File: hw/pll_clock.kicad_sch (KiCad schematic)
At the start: 24 parts, among them J7 BNC, U7 5P49V6965, Y1 25MHz

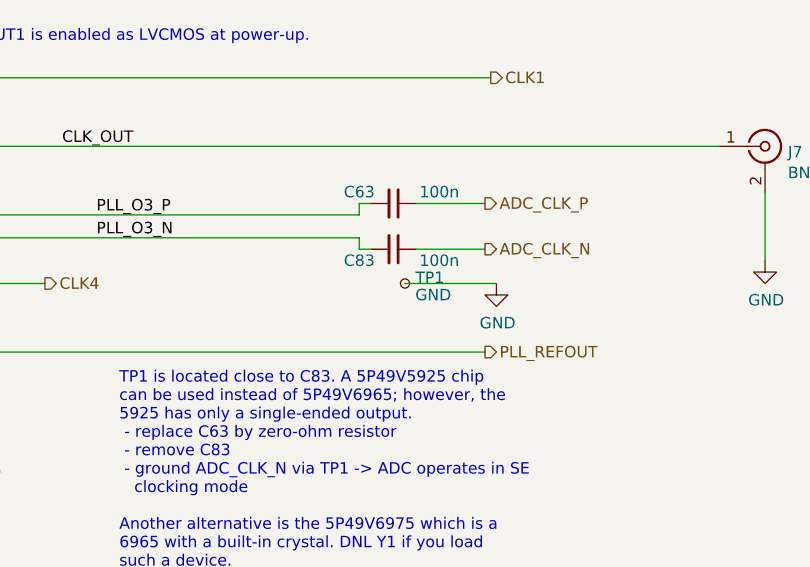
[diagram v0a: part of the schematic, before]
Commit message: updated parts assignments
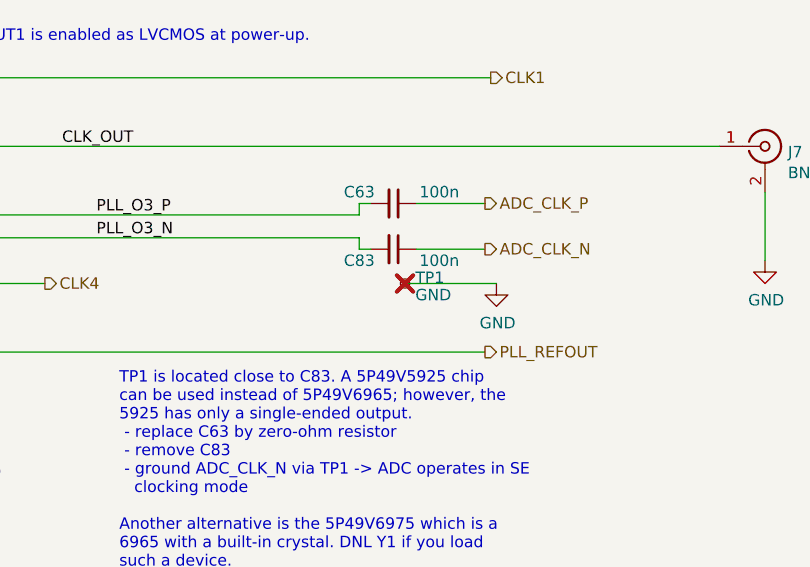
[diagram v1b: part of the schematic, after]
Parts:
- R11: Manufacturer (none) -> Stackpole; Part (none) -> RMCF0603FT2K94
- R118, R24, R27: Manufacturer (none) -> Stackpole; Part (none) -> RMCF0603FT33R0
- R17: Manufacturer (none) -> Stackpole; Part (none) -> RMCF0603FT301R
- R18: Manufacturer (none) -> Stackpole; Part (none) -> RMCF0603FT590R
- TP1: now not fitted; now left out of the parts list
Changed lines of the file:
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@@
 			)
 		)
-		(property "Part" ""
+		(property "Part" "RMCF0603FT33R0"
 			(at 163.83 81.28 90)
 			(effects
@@
 			)
 		)
-		(property "Manufacturer" ""
+		(property "Manufacturer" "Stackpole"
 			(at 163.83 81.28 90)
 			(effects
@@
 			)
 		)
-		(property "Datasheet" " ~"
+		(property "Datasheet" "~"
 			(at 254.635 81.28 0)
 			(effects
@@
 			)
 		)
-		(property "Part" ""
+		(property "Part" "RMCF0603FT33R0"
 			(at 163.83 73.66 90)
 			(effects
@@
 			)
 		)
-		(property "Manufacturer" ""
+		(property "Manufacturer" "Stackpole"
 			(at 163.83 73.66 90)
 			(effects
@@
 			)
 		)
-		(property "Part" ""
+		(property "Part" "RMCF0603FT33R0"
 			(at 163.83 96.52 90)
 			(effects
@@
 			)
 		)
-		(property "Manufacturer" ""
+		(property "Manufacturer" "Stackpole"
 			(at 163.83 96.52 90)
 			(effects
@@
 			)
 		)
-		(property "Part" ""
+		(property "Part" "RMCF0603FT301R"
 			(at 82.042 78.486 90)
 			(effects
@@
 			)
 		)
-		(property "Manufacturer" ""
+		(property "Manufacturer" "Stackpole"
 			(at 82.042 78.486 90)
 			(effects
@@
 			)
 		)
-		(property "Part" ""
+		(property "Part" "RMCF0603FT590R"
 			(at 82.042 71.12 90)
 			(effects
@@
 			)
 		)
-		(property "Manufacturer" ""
+		(property "Manufacturer" "Stackpole"
 			(at 82.042 71.12 90)
 			(effects
@@
 		(unit 1)
 		(exclude_from_sim no)
-		(in_bom yes)
-		(on_board yes)
-		(dnp no)
+		(in_bom no)
+		(on_board yes)
+		(dnp yes)
 		(fields_autoplaced yes)
 		(property "Reference" "TP1"
@@
 			)
 		)
-		(property "Part" ""
+		(property "Part" "RMCF0603FT2K94"
 			(at 167.64 110.49 90)
 			(effects
@@
 			)
 		)
-		(property "Manufacturer" ""
+		(property "Manufacturer" "Stackpole"
 			(at 167.64 110.49 90)
 			(effects

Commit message: fixed BOM; added relay drivers
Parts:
- U7: Part 5P49V6965 -> 5P49V6965A000NLGI8
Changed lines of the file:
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@@
 			)
 		)
-		(property "Part" "5P49V6965"
+		(property "Part" "  5P49V6965A000NLGI8"
 			(at 142.24 121.1834 0)
 			(effects

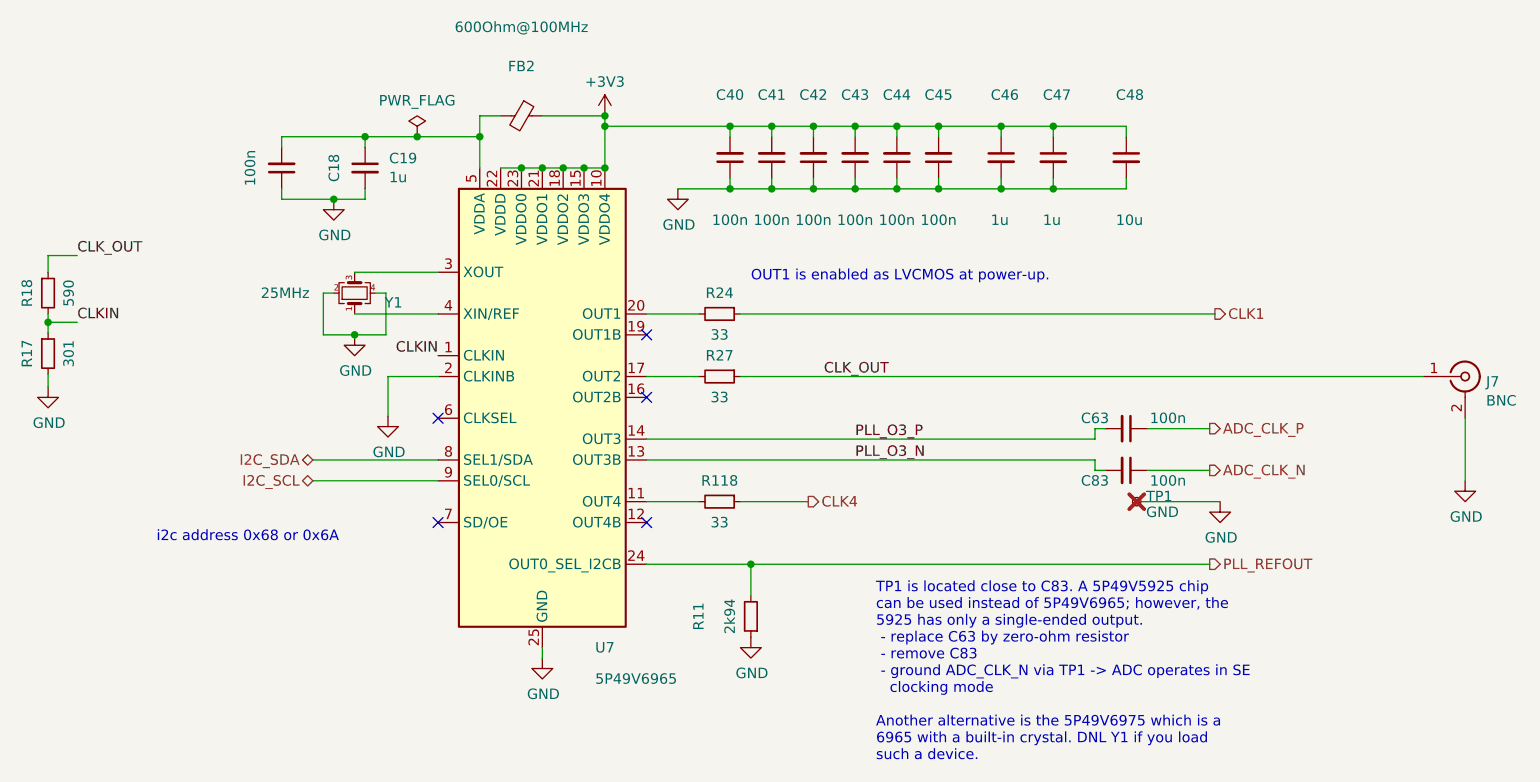
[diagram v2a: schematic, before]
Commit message: connected versaclock CLKSEL to ULPI RSTB (share FPGA pin)
ULPI Rstb is unlikely to be used

Also: - update of kicad to 9.0 (many library footprints updated)
      - added sheet titles, author
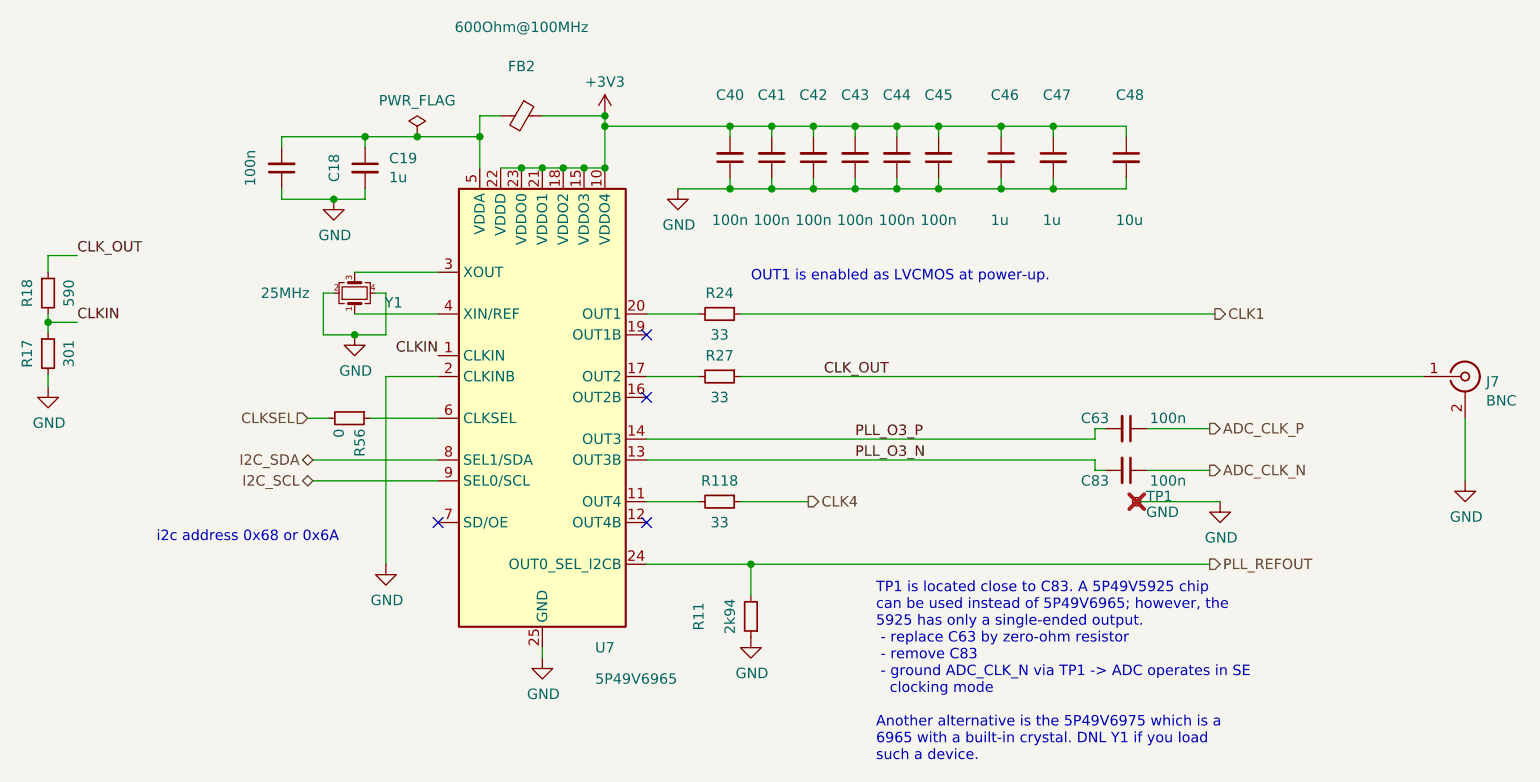
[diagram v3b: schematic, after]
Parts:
- added R56: 0, Resistor_SMD:R_0603_1608Metric, symbol Device:R_Small
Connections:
- net at U7.6 (CLKSEL): now also R56.1
- new net CLKSEL: R56.2
- no-connect marks 5 -> 4
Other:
- company: (none) -> Till Straumann
- title: (none) -> Clock Generator
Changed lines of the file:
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@@
 (kicad_sch
-	(version 20231120)
+	(version 20250114)
 	(generator "eeschema")
-	(generator_version "8.0")
+	(generator_version "9.0")
 	(paper "A4")
+	(title_block
+		(title "Clock Generator")
+		(rev "3.3b")
+		(company "Till Straumann")
+	)
+	(text "TP1 is located close to C83. A 5P49V5925 chip\ncan be used instead of 5P49V6965; however, the\n5925 has only a single-ended output.\n - replace C63 by zero-ohm resistor\n - remove C83\n - ground ADC_CLK_N via TP1 -> ADC operates in SE\n   clocking mode\n\nAnother alternative is the 5P49V6975 which is a\n6965 with a built-in crystal. DNL Y1 if you load\nsuch a device."
+		(exclude_from_sim no)
+		(at 182.88 128.27 0)
+		(effects
+			(font
+				(size 1.27 1.27)
+			)
+			(justify left bottom)
+		)
+	)
+	(text "i2c address 0x68 or 0x6A"
+		(exclude_from_sim no)
+		(at 95.25 101.6 0)
+		(effects
+			(font
+				(size 1.27 1.27)
+			)
+			(justify left bottom)
+		)
+	)
+	(text "OUT1 is enabled as LVCMOS at power-up."
+		(exclude_from_sim no)
+		(at 167.64 69.85 0)
+		(effects
+			(font
+				(size 1.27 1.27)
+			)
+			(justify left bottom)
+		)
+	)
 	(junction
 		(at 82.042 74.676)
@@
 	)
 	(no_connect
-		(at 129.54 86.36)
-	)
-	(no_connect
 		(at 154.94 83.82)
 	)
@@
 	(wire
 		(pts
+			(xy 121.285 86.36) (xy 129.54 86.36)
+		)
+		(stroke
+			(width 0)
+			(type default)
+		)
+	)
+	(wire
+		(pts
 			(xy 134.62 52.07) (xy 134.62 55.88)
 		)
@@
 	(wire
 		(pts
+			(xy 113.665 86.36) (xy 116.205 86.36)
+		)
+		(stroke
+			(width 0)
+			(type default)
+		)
+	)
+	(wire
+		(pts
 			(xy 142.24 114.3) (xy 142.24 115.57)
 		)
@@
 	(wire
 		(pts
-			(xy 123.444 81.28) (xy 123.444 86.106)
+			(xy 123.19 81.28) (xy 123.19 104.14)
 		)
 		(stroke
@@
 	(wire
 		(pts
-			(xy 129.54 81.28) (xy 123.444 81.28)
+			(xy 129.54 81.28) (xy 123.19 81.28)
 		)
 		(stroke
@@
 		)
 	)
-	(text "TP1 is located close to C83. A 5P49V5925 chip\ncan be used instead of 5P49V6965; however, the\n5925 has only a single-ended output.\n - replace C63 by zero-ohm resistor\n - remove C83\n - ground ADC_CLK_N via TP1 -> ADC operates in SE\n   clocking mode\n\nAnother alternative is the 5P49V6975 which is a\n6965 with a built-in crystal. DNL Y1 if you load\nsuch a device."
-		(exclude_from_sim no)
-		(at 182.88 128.27 0)
-		(effects
-			(font
-				(size 1.27 1.27)
-			)
-			(justify left bottom)
-		)
-	)
-	(text "i2c address 0x68 or 0x6A"
-		(exclude_from_sim no)
-		(at 95.25 101.6 0)
-		(effects
-			(font
-				(size 1.27 1.27)
-			)
-			(justify left bottom)
-		)
-	)
-	(text "OUT1 is enabled as LVCMOS at power-up."
-		(exclude_from_sim no)
-		(at 167.64 69.85 0)
-		(effects
-			(font
-				(size 1.27 1.27)
-			)
-			(justify left bottom)
-		)
-	)
 	(label "CLK_OUT"
 		(at 85.598 66.548 0)
@@
 		)
 	)
+	(hierarchical_label "CLKSEL"
+		(shape input)
+		(at 113.665 86.36 180)
+		(effects
+			(font
+				(size 1.27 1.27)
+			)
+			(justify right)
+		)
+	)
 	(hierarchical_label "ADC_CLK_N"
 		(shape output)
@@
 	)
 	(symbol
+		(lib_id "Device:R_Small")
+		(at 118.745 86.36 270)
+		(unit 1)
+		(exclude_from_sim no)
+		(in_bom yes)
+		(on_board yes)
+		(dnp no)
+		(property "Reference" "R56"
+			(at 120.015 87.63 0)
+			(effects
+				(font
+					(size 1.27 1.27)
+				)
+				(justify left)
+			)
+		)
+		(property "Value" "0"
+			(at 117.475 87.63 0)
+			(effects
+				(font
+					(size 1.27 1.27)
+				)
+				(justify left)
+			)
+		)
+		(property "Footprint" "Resistor_SMD:R_0603_1608Metric"
+			(at 118.745 86.36 0)
+			(effects
+				(font
+					(size 1.27 1.27)
+				)
+				(hide yes)
+			)
+		)
+		(property "Datasheet" "~"
+			(at 118.745 86.36 0)
+			(effects
+				(font
+					(size 1.27 1.27)
+				)
+				(hide yes)
+			)
+		)
+		(property "Description" ""
+			(at 118.745 86.36 0)
+			(effects
+				(font
+					(size 1.27 1.27)
+				)
+				(hide yes)
+			)
+		)
+		(property "Manufacturer" "Stackpole"
+			(at 118.745 86.36 0)
+			(effects
+				(font
+					(size 1.27 1.27)
+				)
+				(hide yes)
+			)
+		)
+		(property "Part" "  RMCF0603ZT0R00"
+			(at 118.745 86.36 0)
+			(effects
+				(font
+					(size 1.27 1.27)
+				)
+				(hide yes)
+			)
+		)
+		(pin "1"
+		)
+		(pin "2"
+		)
+		(instances
+			(project "usbadc"
+				(path "/7c8a1f8d-8834-4c9b-aaae-1f231e9b09a1/00000000-0000-0000-0000-000060b16d71"
+					(reference "R56")
+					(unit 1)
+				)
+			)
+		)
+	)
+	(symbol
 		(lib_id "power:GND")
-		(at 123.444 86.106 0)
+		(at 123.19 104.14 0)
 		(unit 1)
 		(exclude_from_sim no)
@@
 		(dnp no)
 		(property "Reference" "#PWR05"
-			(at 123.444 92.456 0)
+			(at 123.19 110.49 0)
 			(effects
 				(font
@@
 		)
 		(property "Value" "GND"
-			(at 123.571 90.5002 0)
+			(at 123.317 108.5342 0)
 			(effects
 				(font
@@
 		)
 		(property "Footprint" ""
-			(at 123.444 86.106 0)
+			(at 123.19 104.14 0)
 			(effects
 				(font
@@
 		)
 		(property "Datasheet" ""
-			(at 123.444 86.106 0)
+			(at 123.19 104.14 0)
 			(effects
 				(font
@@
 		)
 		(property "Description" ""
-			(at 123.444 86.106 0)
+			(at 123.19 104.14 0)
 			(effects
 				(font

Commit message: Added licensing information
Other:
- company: Till Straumann -> Copyright Till Straumann, 2025
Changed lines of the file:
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@@
 		(title "Clock Generator")
 		(rev "3.3b")
-		(company "Till Straumann")
+		(company "Copyright Till Straumann, 2025")
+		(comment 1 "License: CERN-OHL-P v2")
 	)
 	(text "TP1 is located close to C83. A 5P49V5925 chip\ncan be used instead of 5P49V6965; however, the\n5925 has only a single-ended output.\n - replace C63 by zero-ohm resistor\n - remove C83\n - ground ADC_CLK_N via TP1 -> ADC operates in SE\n   clocking mode\n\nAnother alternative is the 5P49V6975 which is a\n6965 with a built-in crystal. DNL Y1 if you load\nsuch a device."
